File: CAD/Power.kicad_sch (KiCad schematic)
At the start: 81 parts, among them U10 AOZ1284, U14 TS30041, U18 AP7330-W5-7, U4 AP7361C-33E-13

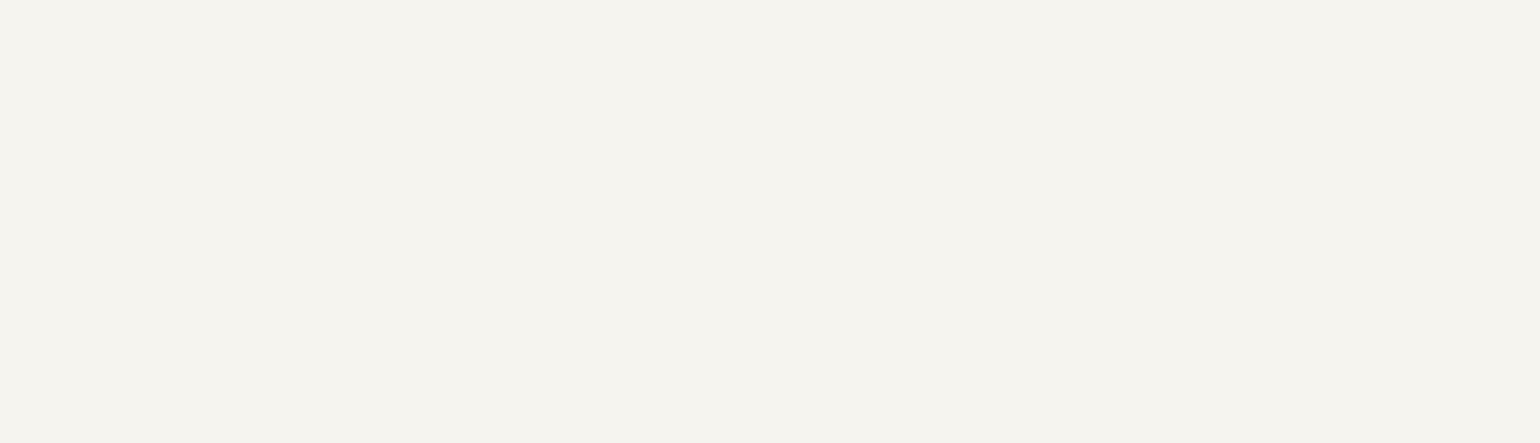
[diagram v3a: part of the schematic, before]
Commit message: TODO: Finish LM5013, find replacement for TS30041
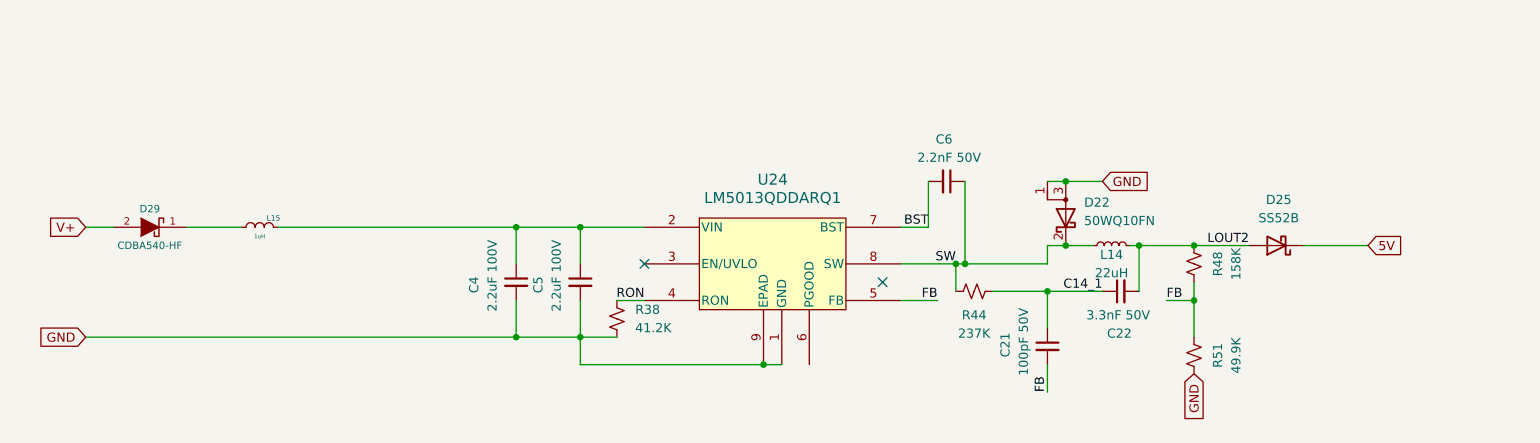
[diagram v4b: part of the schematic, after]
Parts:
- added C21: 100pF 50V, Capacitor_SMD:C_0805_2012Metric, symbol Device:C_Small
- added C22: 3.3nF 50V, Capacitor_SMD:C_0805_2012Metric, symbol Device:C_Small
- added C4, C5: 2.2uF 100V, Capacitor_SMD:C_1210_3225Metric, symbol Device:C_Small
- added C6: 2.2nF 50V, Capacitor_SMD:C_0805_2012Metric, symbol Device:C_Small
- added D22: 50WQ10FN, Package_TO_SOT_SMD:TO-252-2, symbol Device:D_Schottky_AKA
- added D25: SS52B, Diode_SMD:D_SMB, symbol Device:D_Schottky
- added D29: CDBA540-HF, Diode_SMD:D_SMA, symbol Duet3:CDBA540
- added L14: 22uH, Inductor_SMD:L_Sunlord_SWRB1207S, symbol Device:L_Small
- added L15: 1uH, Inductor_SMD:L_1210_3225Metric, symbol Duet3:L_MINI
- added R38: 41.2K, Resistor_SMD:R_0402_1005Metric, symbol Device:R_Small_US
- added R44: 237K, Resistor_SMD:R_0603_1608Metric, symbol Device:R_Small_US
- added R48: 158K, Resistor_SMD:R_0603_1608Metric, symbol Device:R_Small_US
- added R51: 49.9K, Resistor_SMD:R_0603_1608Metric, symbol Device:R_Small_US
- added U24: LM5013QDDARQ1, 3DPotter:POWERPAD8_DDA_TEX, symbol 3DPotter:LM5013QDDARQ1
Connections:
- net GND: now also C4.2, C5.2, D22.1 (A), D22.3 (A), R38.2, R51.2, U24.1 (GND), U24.9 (EPAD)
- new net: C4.1, C5.1, L15.1 (A), U24.2 (VIN)
- new net: D29.1 (K), L15.2 (B)
- new net 5V: D25.1 (K)
- new net BST: C6.2, U24.7 (BST)
- new net C14_1: C21.1, C22.1, R44.1
- new net FB: C21.2, R48.2, R51.1, U24.5 (FB)
- new net LOUT2: C22.2, D25.2 (A), L14.2, R48.1
- new net RON: R38.1, U24.4 (RON)
- new net SW: C6.1, D22.2 (K), L14.1, R44.2, U24.8 (SW)
- new net V+: D29.2 (A)
- no-connect marks 1 -> 3

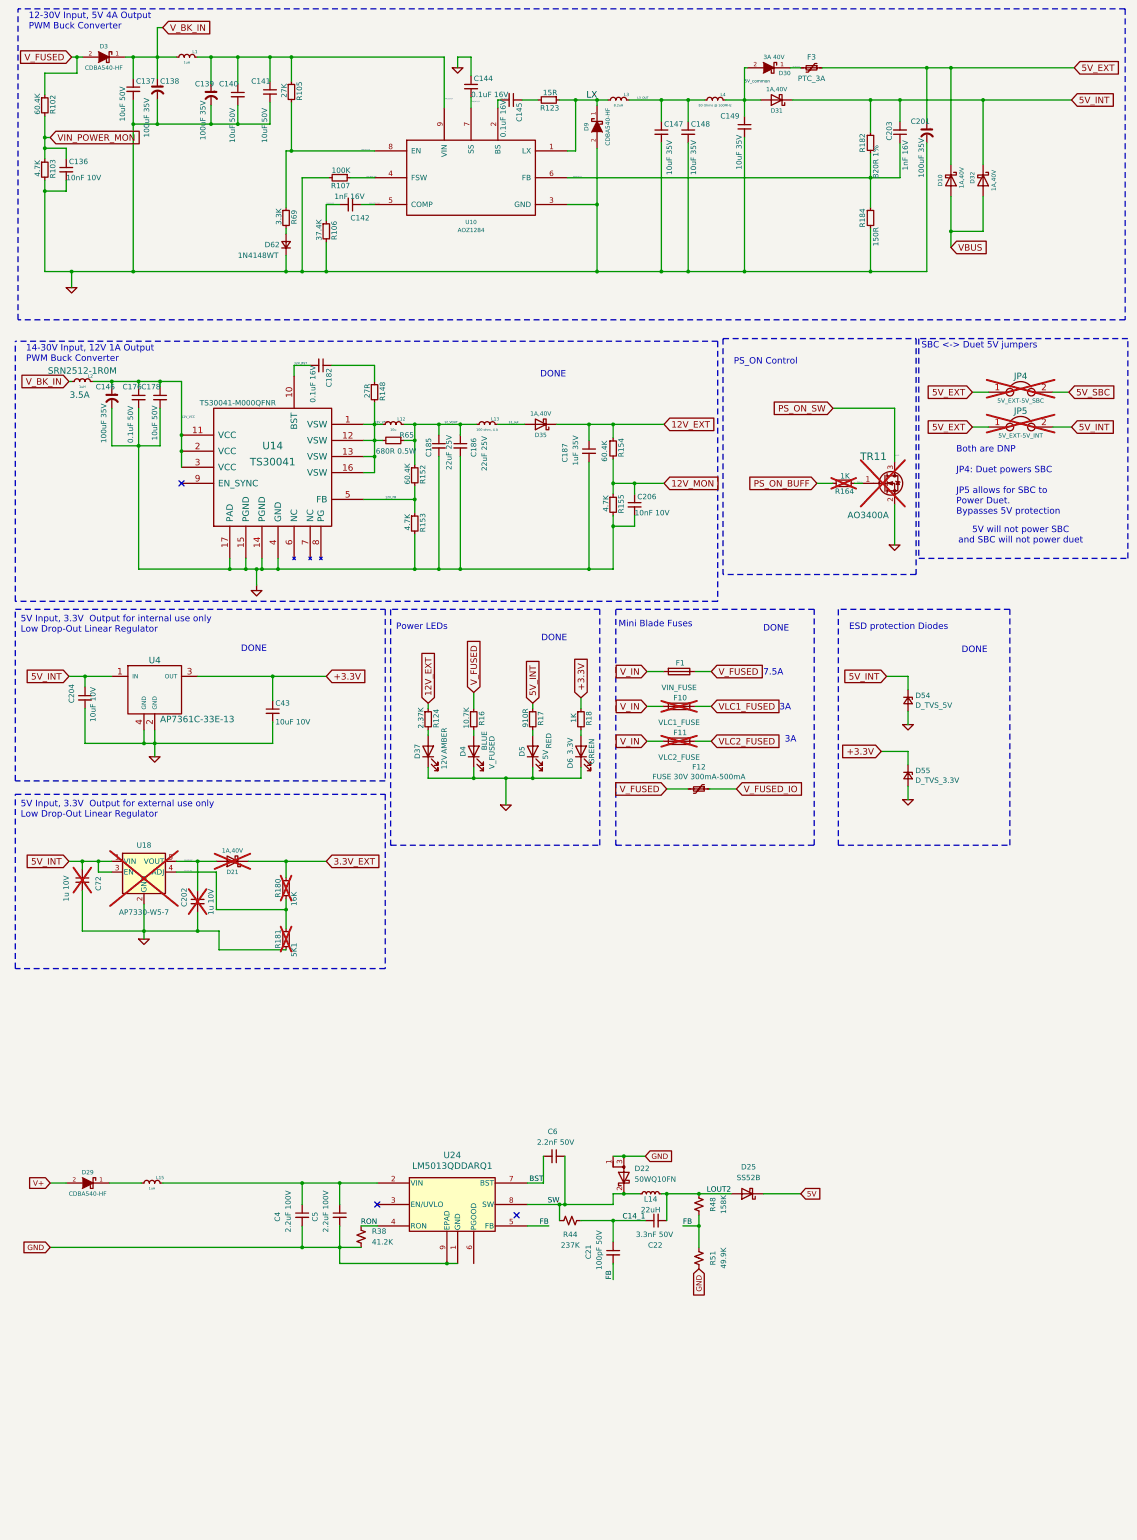
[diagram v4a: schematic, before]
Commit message: Remove 12V Buck Converter
No need for it, unnecessarily complicates design, plus I dont feel like designing 2 Buck Converter layouts
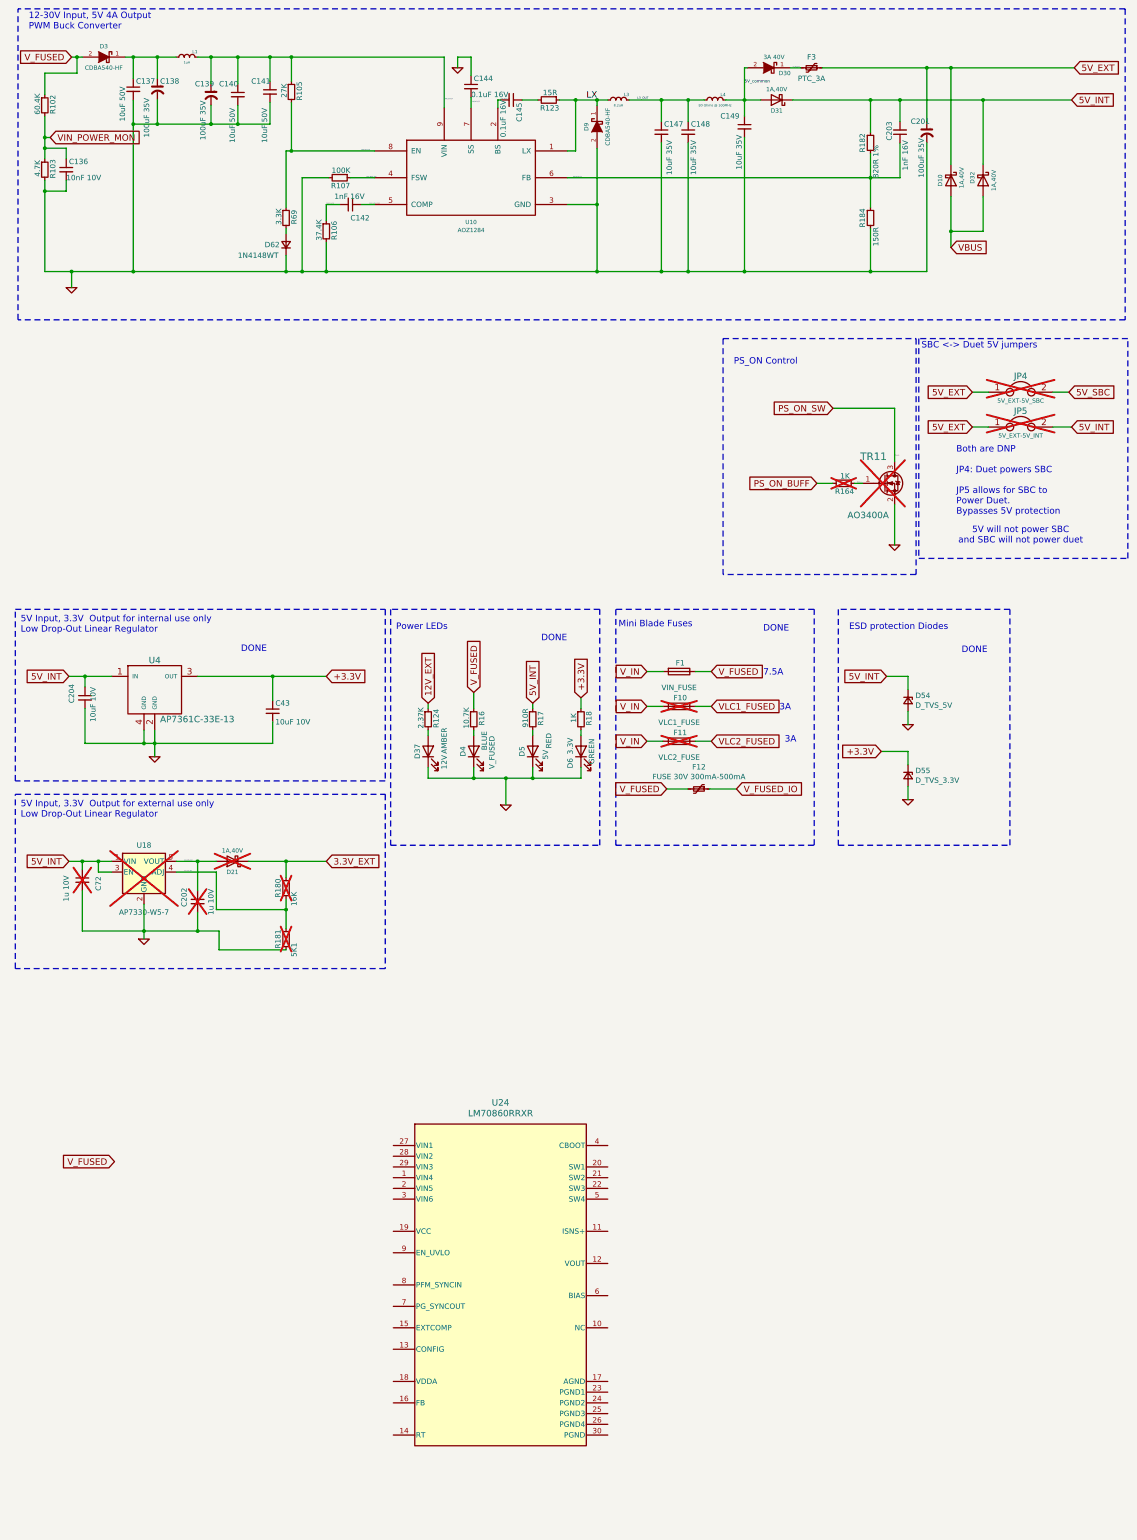
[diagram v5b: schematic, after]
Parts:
- removed C146: 100uF 35V, Capacitor_SMD:CP_Elec_6.3x7.7, symbol Duet3:C_POL
- removed C176: 0.1uF 50V, Capacitor_SMD:C_0603_1608Metric_Wbry, symbol Device:C_Small
- removed C178: 10uF 50V, Capacitor_SMD:C_1206_3216Metric, symbol Device:C_Small
- removed C182: 0.1uF 16V, Capacitor_SMD:C_0402_1005Metric_Wbry, symbol Device:C_Small
- removed C185, C186: 22uF 25V, Capacitor_SMD:C_0805_2012Metric, symbol Device:C_Small
- removed C187: 1uF 35V, Capacitor_SMD:C_0603_1608Metric_Wbry, symbol Device:C_Small
- removed C206: 10nF 10V, Capacitor_SMD:C_0402_1005Metric, symbol Device:C_Small
- removed C21: 100pF 50V, Capacitor_SMD:C_0805_2012Metric, symbol Device:C_Small
- removed C22: 3.3nF 50V, Capacitor_SMD:C_0805_2012Metric, symbol Device:C_Small
- removed C4, C5: 2.2uF 100V, Capacitor_SMD:C_1210_3225Metric, symbol Device:C_Small
- removed C6: 2.2nF 50V, Capacitor_SMD:C_0805_2012Metric, symbol Device:C_Small
- removed D22: 50WQ10FN, Package_TO_SOT_SMD:TO-252-2, symbol Device:D_Schottky_AKA
- removed D25: SS52B, Diode_SMD:D_SMB, symbol Device:D_Schottky
- removed D29: CDBA540-HF, Diode_SMD:D_SMA, symbol Duet3:CDBA540
- removed D35: 1A,40V, Diode_SMD:D_SOD-123F, symbol Device:D_Schottky
- removed L12: 10u, Carters_Various_Bits_and_Pieces:SMD_5.2x5.7mm_1.0x2.0mm, symbol Duet3:L_MINI
- removed L13: 100 ohm, 4 A, Inductor_SMD:L_1206_3216Metric, symbol Duet3:L_MINI
- removed L14: 22uH, Inductor_SMD:L_Sunlord_SWRB1207S, symbol Device:L_Small
- removed L15, L2: 1uH, Inductor_SMD:L_1210_3225Metric, symbol Duet3:L_MINI
- removed R148: 27R, Resistor_SMD:R_0402_1005Metric_Wbry, symbol Device:R_Small
- removed R152, R154: 60.4K, Resistor_SMD:R_0402_1005Metric_Wbry, symbol Device:R_Small
- removed R153, R155: 4.7K, Resistor_SMD:R_0402_1005Metric_Wbry, symbol Device:R_Small
- removed R38: 41.2K, Resistor_SMD:R_0402_1005Metric, symbol Device:R_Small_US
- removed R44: 237K, Resistor_SMD:R_0603_1608Metric, symbol Device:R_Small_US
- removed R48: 158K, Resistor_SMD:R_0603_1608Metric, symbol Device:R_Small_US
- removed R51: 49.9K, Resistor_SMD:R_0603_1608Metric, symbol Device:R_Small_US
- removed R65: 680R 0.5W, Resistor_SMD:R_0805_2012Metric, symbol Device:R_Small
- removed U14: TS30041, Carters_Various_Bits_and_Pieces:QFN-16-1EP_3x3mm_P0.5mm_EP1.8x1.8mm, symbol Duet3:TS30042
- removed U24: LM5013QDDARQ1, 3DPotter:POWERPAD8_DDA_TEX, symbol 3DPotter:LM5013QDDARQ1
- added U24: LM70860RRXR, 3DPotter:RRX0029B-MFG, symbol 3DPotter:LM70860RRXR
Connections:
- net V_BK_IN: no longer names the net of C137.1, C138.1, D3.1 (K), L1.2 (B)
- no-connect marks 3 -> 0
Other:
- note removed: "14-30V Input, 12V 1A Output PWM Buck Converter"
